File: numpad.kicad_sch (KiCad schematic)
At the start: 17 parts, among them P1 USB_C_Plug_USB2.0, SW1 SW_Push, U1 ATmega32U4-A, Y1 16MHz

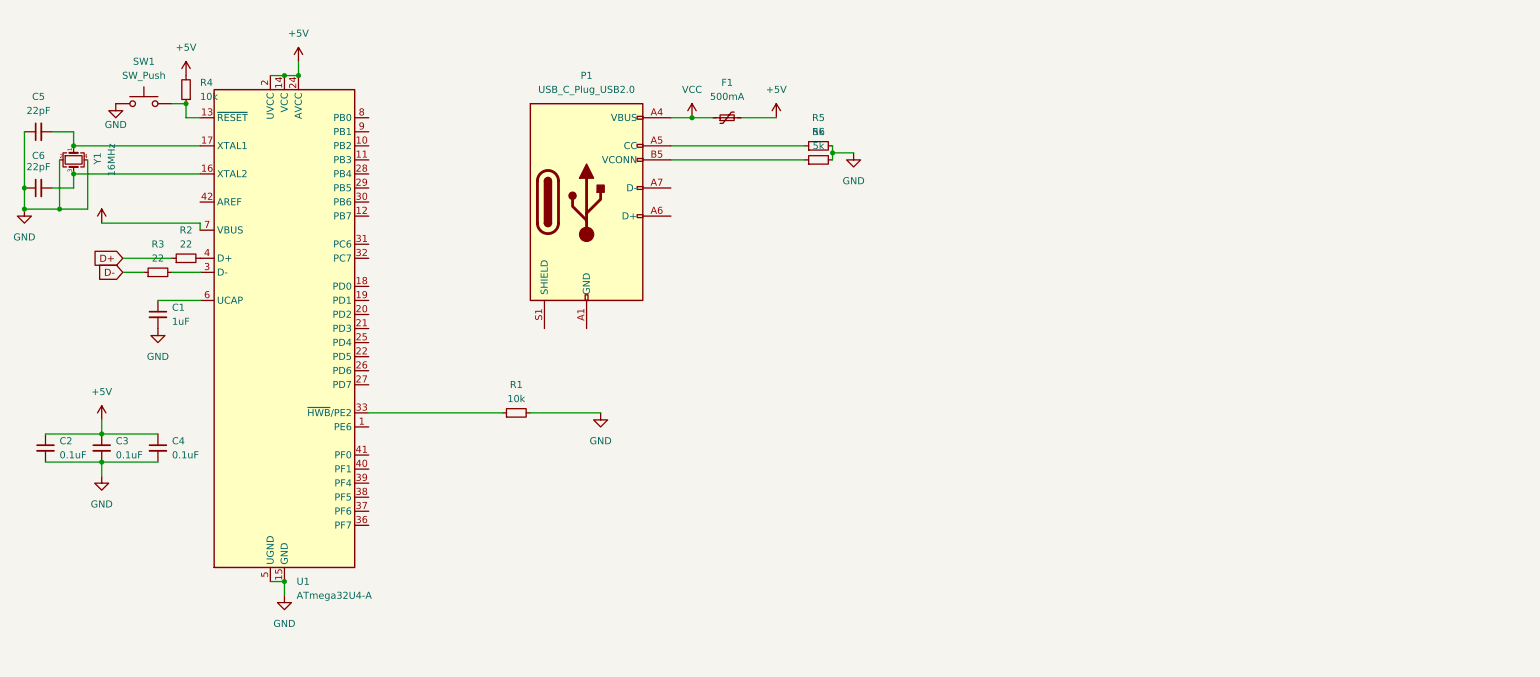
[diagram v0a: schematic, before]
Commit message: Add submodules
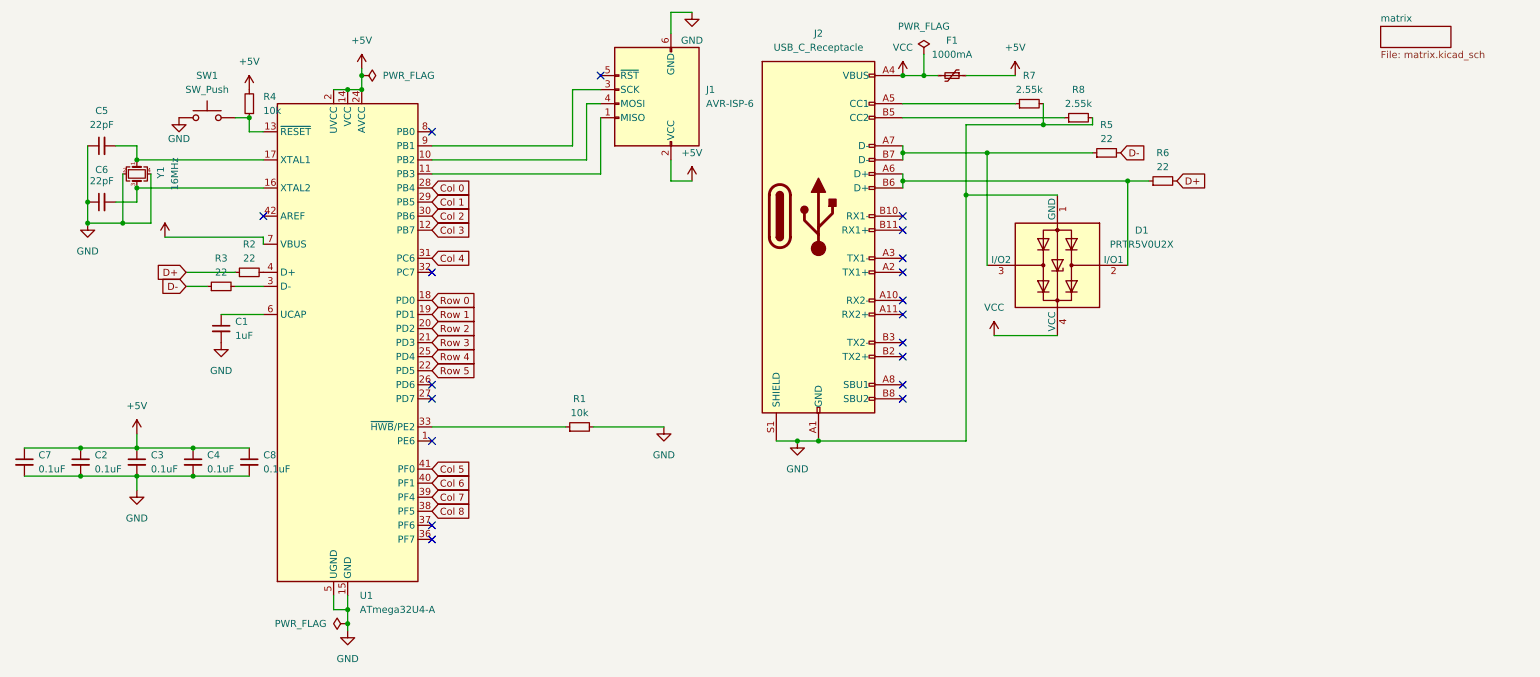
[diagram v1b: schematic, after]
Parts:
- removed P1: USB_C_Plug_USB2.0, symbol Connector:USB_C_Plug_USB2.0
- added C7, C8: 0.1uF, Capacitor_SMD:C_0201_0603Metric, symbol Device:C_Small
- added D1: PRTR5V0U2X, Package_TO_SOT_SMD:SOT-143, symbol Power_Protection:PRTR5V0U2X
- added J1: AVR-ISP-6, symbol Connector:AVR-ISP-6
- added J2: USB_C_Receptacle, Connector_USB:USB_C_Receptacle_HRO_TYPE-C-31-M-12, symbol Connector:USB_C_Receptacle
- added R7, R8: 2.55k, Resistor_SMD:R_0201_0603Metric, symbol Device:R_Small
- C1, C2, C3, C4, C5, C6: footprint (none) -> Capacitor_SMD:C_0201_0603Metric
- F1: value 500mA -> 1000mA; footprint (none) -> Fuse:Fuse_0402_1005Metric
- R1, R2, R3, R4: footprint (none) -> Resistor_SMD:R_0201_0603Metric
- R5, R6: value 5k -> 22; footprint (none) -> Resistor_SMD:R_0201_0603Metric
- Y1: footprint (none) -> Crystal:Crystal_SMD_0603-2Pin_6.0x3.5mm
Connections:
- net +5V: now also F1.1, C7.1, C8.1, J1.2 (VCC); no longer F1.2
- net D+: now also R6.2
- net D-: now also R5.2
- net GND: now also C7.2, C8.2, D1.1 (GND), J1.6 (GND), J2.A1 (GND), J2.A12 (GND), J2.B1 (GND), J2.B12 (GND), J2.S1 (SHIELD), R7.2, R8.2; no longer R5.2, R6.2
- net VCC: now also F1.2, D1.4 (VCC), J2.A4 (VBUS), J2.A9 (VBUS), J2.B4 (VBUS), J2.B9 (VBUS); no longer F1.1
- net at R5.1: now also D1.3 (I/O2), J2.A7 (D-), J2.B7 (D-)
- net at R6.1: now also D1.2 (I/O1), J2.A6 (D+), J2.B6 (D+)
- net at U1.10 (PB2): now also J1.4 (MOSI)
- net at U1.11 (PB3): now also J1.1 (MISO)
- net Col 3: now reaches U1.12 (PB7)
- net Row 0: now reaches U1.18 (PD0)
- net Row 1: now reaches U1.19 (PD1)
- net Row 2: now reaches U1.20 (PD2)
- net Row 3: now reaches U1.21 (PD3)
- net Row 5: now reaches U1.22 (PD5)
- net Row 4: now reaches U1.25 (PD4)
- net Col 0: now reaches U1.28 (PB4)
- net Col 1: now reaches U1.29 (PB5)
- net Col 2: now reaches U1.30 (PB6)
- net Col 4: now reaches U1.31 (PC6)
- net Col 8: now reaches U1.38 (PF5)
- net Col 7: now reaches U1.39 (PF4)
- net Col 6: now reaches U1.40 (PF1)
- net Col 5: now reaches U1.41 (PF0)
- net at U1.9 (PB1): now also J1.3 (SCK)
- new net: J2.B5 (CC2), R8.1
- new net: J2.A5 (CC1), R7.1
- no-connect marks 0 -> 19
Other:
- added sheet matrix (matrix.kicad_sch)
- moved on the sheet: C1, C2, C3, C4, C5, C6, R1, R2, R3, R4, SW1, U1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
